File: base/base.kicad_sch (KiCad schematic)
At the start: 0 parts

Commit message: base: DF40 receptacle + DIP48 socket, schematic drawn and wired
Board B goes DF40 mezzanine -> 48-pin DIP socket (female). The XGecu
adapter carries the male DIP48 pins and inserts from above; both are
viewed from the top so the socket is not mirrored, unlike the DF40 pair.

Stack height is 1.5 mm, forced by the plug already on the carrier.
DF40GB is the shielded family, and per the DF40 catalog it offers 30
positions at 1.5 mm only, with DF40GB(1.5)-30DS-0.4V(51) as the sole
mating receptacle. No DF40 family reaches 4.0 mm at 30 positions; that
starts at 50. Unshielded DF40C/HC would reach 3.5 mm but need a new plug
on the carrier.

New parts:
- HIROSE_DF40GB-30DS-0.4V_51_ footprint, from catalog p.12 Recommended
  PCB Pattern: signal 0.2 x 0.70 at y +-1.54, ground 0.28 x 0.72 at
  x +-3.24 / y +-1.68. Mirrored in X, pin 1 at +X, for the face-to-face
  mate.
- DIP-48_Socket_W15.24mm_P2.54mm, 48 THT, 0.9 drill / 1.6 pad, 0.6in
  rows, 58.42 mm pin 1 to pin 24.
- DF40GB-30DS-0.4V_51_ and DIP-48_Socket symbols.
- base/lib registered in both library tables.

base.kicad_sch: J1 receptacle, J2 socket, 10k pull-ups on RY//BY and
/WP, 1 uF bulk + 100 nF, PWR_FLAGs since power arrives through J2.
ERC 0 violations. 17 nets, every one cross-checked against both tables
in docs/connector-pinout.md.

Docs corrected: the "schematic is drawn and wired" claim, the netclass
pattern table, the stack height, and the mating-face description.

Co-Authored-By: Claude Opus 5 <noreply@anthropic.com>
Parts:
- added C1: 1uF, Capacitor_SMD:C_0603_1608Metric, symbol Device:C
- added C2: 100nF, Capacitor_SMD:C_0402_1005Metric, symbol Device:C
- added J1: DF40GB(1.5)-30DS-0.4V(51), Connector_Hirose_DF40:HIROSE_DF40GB-30DS-0.4V_51_, symbol carrier:DF40GB-30DS-0.4V_51_
- added J2: DIP-48_Socket, base:DIP-48_Socket_W15.24mm_P2.54mm, symbol base:DIP-48_Socket
- added R1, R2: 10k, Resistor_SMD:R_0402_1005Metric, symbol Device:R
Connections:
- new net ALE: J1.12, J2.17 (ALE)
- new net CLE: J1.8, J2.16 (CLE)
- new net GND: C1.2, C2.2, J1.10, J1.11, J1.14, J1.18, J1.2, J1.22, J1.23, J1.26, J1.27, J1.3, J1.30, J1.6, J1.7, J1.G1 (GND), J1.G2 (GND), J1.G3 (GND), J1.G4 (GND), J2.13 (VSS), J2.36 (VSS)
- new net IO1: J1.1, J2.29 (I/O1)
- new net IO2: J1.5, J2.30 (I/O2)
- new net IO3: J1.9, J2.31 (I/O3)
- new net IO4: J1.13, J2.32 (I/O4)
- new net IO5: J1.17, J2.41 (I/O5)
- new net IO6: J1.21, J2.42 (I/O6)
- new net IO7: J1.25, J2.43 (I/O7)
- new net IO8: J1.29, J2.44 (I/O8)
- new net RY//BY: J1.28, J2.7 (RY/~{BY}), R1.2
- new net VCC: C1.1, C2.1, J1.15, J1.19, J2.12 (VCC), J2.37 (VCC), R1.1, R2.1
- new net /CE: J1.4, J2.9 (~{CE})
- new net /RE: J1.20, J2.8 (~{RE})
- new net /WE: J1.16, J2.18 (~{WE})
- new net /WP: J1.24, J2.19 (~{WP}), R2.2
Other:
- company: (none) -> Alex Gompper
- title: (none) -> DF40 Mezzanine to DIP48 Socket

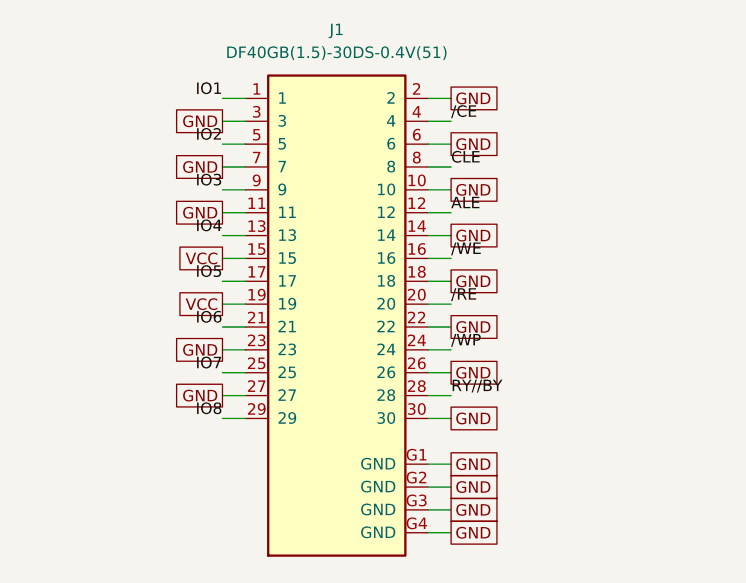
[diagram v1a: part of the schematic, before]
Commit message: Re-derive the J1 pinout from ball geometry; regenerate both schematics
Alex asked to optimise J1's pin assignment for the BGA fanout, and to
consider routing on the inner layers working back from J1 rather than
out from U1. Working backwards is what produced the result.

The topology falls out of the ball map with no slack. The VFBGA67's 20
used balls split into an upper cluster (columns 2-4: IO1-IO4 plus
CLE/RE/ALE/WP) and a lower one (columns 5-7: IO5-IO8, CE/WE/RY-BY and
both VCC balls) - exactly 8 and 7 signals. J1's odd row has exactly 8
signal slots and its even row exactly 7. So the row assignment is
forced, and within a row ordering by ball x makes the escape fan out
monotonically. IO1-IO8 are no longer in pin order on the connector;
that is deliberate and safe, because the rule that matters is the
end-to-end mapping, not the connector order.

Measured against the previous pinout with a routing-aware cost model
(octilinear where clear, around-the-end where the connector body is in
the way): 141.2 mm -> 74.8 mm of point-to-point routing, IO skew
10.32 mm -> 2.94 mm, and around-the-end paths 11 -> 5. Constraining the
bus to stay contiguous recovers almost none of that (139.6 mm), because
the IO balls all sit on one side while a monotonic bus spans J1's full
5.6 mm.

Skew was not the reason to do this. 10 mm is ~62 ps on FR4 against a
25 ns read cycle. The win is copper length and via count.

tools/pinout.py is now the single source: it carries the table and a
checker for the checkerboard invariant (no signal adjacent to or
opposite another signal) and the net set. Both schematics were
generated from it. Verified: carrier ERC 0, base ERC 0, both J1s match
the table, U1 matches the datasheet ball map, J2 matches the TSOP48
map, and IOn traces ball -> J1 pin -> TSOP48 pin end to end.

Carrier PCB carries placement, net re-import and the BGA escape (20/20
balls, DRC 0 errors). The J1 fanout is NOT routed in this commit - see
the next commit message / handoff for w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
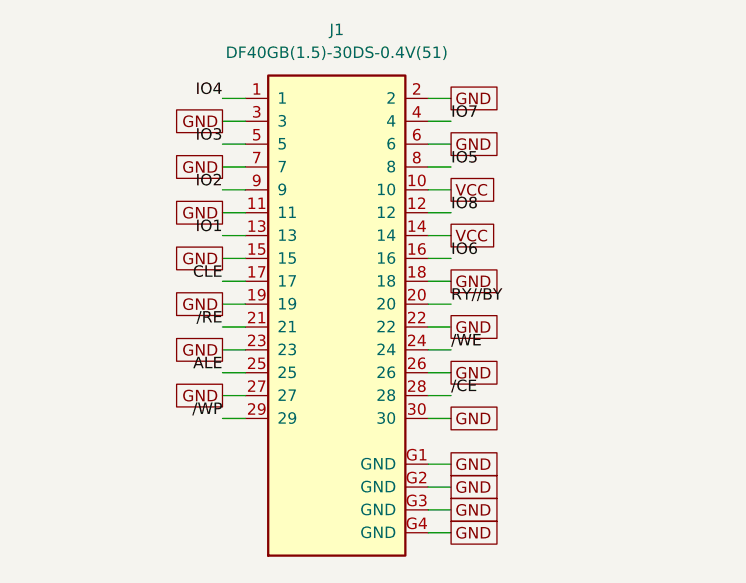
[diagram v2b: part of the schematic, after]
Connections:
- net ALE: now also J1.25; no longer J1.12
- net CLE: now also J1.17; no longer J1.8
- net GND: now also J1.15, J1.19; no longer J1.10, J1.14
- net IO1: now also J1.13; no longer J1.1
- net IO2: now also J1.9; no longer J1.5
- net IO3: now also J1.5; no longer J1.9
- net IO4: now also J1.1; no longer J1.13
- net IO5: now also J1.8; no longer J1.17
- net IO6: now also J1.16; no longer J1.21
- net IO7: now also J1.4; no longer J1.25
- net IO8: now also J1.12; no longer J1.29
- net RY//BY: now also J1.20; no longer J1.28
- net VCC: now also J1.10, J1.14; no longer J1.15, J1.19
- net /CE: now also J1.28; no longer J1.4
- net /RE: now also J1.21; no longer J1.20
- net /WE: now also J1.24; no longer J1.16
- net /WP: now also J1.29; no longer J1.24

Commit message: Carrier fully routed; propagate the VCC pin move to base and the docs
Alex routed the carrier: 0 DRC violations, 0 unconnected, one via per
signal net (20 total), uniform 0.15 mm tracks, teardrops on every
via/pad transition, GND poured on all four layers.

While routing he moved VCC from J1 pin 14 to pin 6, which is the right
call - pin 6's x lines up with the VCC ball H5, and pin 10 already lined
up with G7. But the change landed on the carrier only, so pin 6 was VCC
on one board and GND on the other, and pin 14 the reverse. Mated, that
is VCC shorted to GND through two pins.

Neither project can catch this: they are separate KiCad projects, so
each one's ERC and DRC pass happily. This is exactly the failure the
"single source of truth" note in the pinout doc exists to prevent.

Adopted the carrier's version as canonical: tools/pinout.py now has
VCC on 6 and 10, base regenerated from it, doc table updated. The
checkerboard invariant still holds. Verified both J1s now agree on all
34 pins including the G tabs.

carrier ERC 0, base ERC 0, carrier DRC 0 violations / 0 unconnected.

Co-Authored-By: Claude Opus 5 <noreply@anthropic.com>
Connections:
- net GND: now also J1.14; no longer J1.6
- net VCC: now also J1.6; no longer J1.14
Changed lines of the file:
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@@
 		(property "Value" "DF40GB(1.5)-30DS-0.4V(51)" (at 63.5 40.64 0) (effects (font (size 1.27 1.27))))
 		(property "Footprint" "Connector_Hirose_DF40:HIROSE_DF40GB-30DS-0.4V_51_" (at 63.5 63.5 0) (effects (font (size 1.27 1.27)) (hide yes)))
-		(instances (project "base" (path "/5f6296ef-f47b-4b20-84d4-3df797b20810" (reference "J1") (unit 1))))
+		(instances (project "base" (path "/14e6b38a-f306-41d1-a4e0-ab6ee141c397" (reference "J1") (unit 1))))
 	)
 	(wire (pts (xy 50.8 45.72) (xy 53.34 45.72)) (stroke (width 0) (type default)))
@@
 	(label "IO3" (at 50.8 50.8 0) (effects (font (size 1.27 1.27)) (justify right bottom)))
 	(wire (pts (xy 73.66 50.8) (xy 76.2 50.8)) (stroke (width 0) (type default)))
-	(global_label "GND" (shape passive) (at 76.2 50.8 0) (effects (font (size 1.27 1.27)) (justify left)))
+	(global_label "VCC" (shape passive) (at 76.2 50.8 0) (effects (font (size 1.27 1.27)) (justify left)))
 	(wire (pts (xy 50.8 53.339999999999996) (xy 53.34 53.339999999999996)) (stroke (width 0) (type default)))
 	(global_label "GND" (shape passive) (at 50.8 53.339999999999996 0) (effects (font (size 1.27 1.27)) (justify right)))
@@
 	(label "IO1" (at 50.8 60.96 0) (effects (font (size 1.27 1.27)) (justify right bottom)))
 	(wire (pts (xy 73.66 60.96) (xy 76.2 60.96)) (stroke (width 0) (type default)))
-	(global_label "VCC" (shape passive) (at 76.2 60.96 0) (effects (font (size 1.27 1.27)) (justify left)))
+	(global_label "GND" (shape passive) (at 76.2 60.96 0) (effects (font (size 1.27 1.27)) (justify left)))
 	(wire (pts (xy 50.8 63.5) (xy 53.34 63.5)) (stroke (width 0) (type default)))
 	(global_label "GND" (shape passive) (at 50.8 63.5 0) (effects (font (size 1.27 1.27)) (justify right)))
@@
 		(property "Value" "DIP-48_Socket" (at 152.4 41.3 0) (effects (font (size 1.27 1.27))))
 		(property "Footprint" "base:DIP-48_Socket_W15.24mm_P2.54mm" (at 152.4 50.8 0) (effects (font (size 1.27 1.27)) (hide yes)))
-		(instances (project "base" (path "/5f6296ef-f47b-4b20-84d4-3df797b20810" (reference "J2") (unit 1))))
+		(instances (project "base" (path "/14e6b38a-f306-41d1-a4e0-ab6ee141c397" (reference "J2") (unit 1))))
 	)
 	(wire (pts (xy 149.86 66.03999999999999) (xy 152.4 66.03999999999999)) (stroke (width 0) (type default)))
@@
 		(property "Value" "10k" (at 34.88 128.27 0) (effects (font (size 1.27 1.27))))
 		(property "Footprint" "Resistor_SMD:R_0402_1005Metric" (at 30.48 127.0 0) (effects (font (size 1.27 1.27)) (hide yes)))
-		(instances (project "base" (path "/5f6296ef-f47b-4b20-84d4-3df797b20810" (reference "R1") (unit 1))))
+		(instances (project "base" (path "/14e6b38a-f306-41d1-a4e0-ab6ee141c397" (reference "R1") (unit 1))))
 	)
 	(wire (pts (xy 30.48 123.19) (xy 30.48 120.65)) (stroke (width 0) (type default)))
@@
 		(property "Value" "10k" (at 50.12 128.27 0) (effects (font (size 1.27 1.27))))
 		(property "Footprint" "Resistor_SMD:R_0402_1005Metric" (at 45.72 127.0 0) (effects (font (size 1.27 1.27)) (hide yes)))
-		(instances (project "base" (path "/5f6296ef-f47b-4b20-84d4-3df797b20810" (reference "R2") (unit 1))))
+		(instances (project "base" (path "/14e6b38a-f306-41d1-a4e0-ab6ee141c397" (reference "R2") (unit 1))))
 	)
 	(wire (pts (xy 45.72 123.19) (xy 45.72 120.65)) (stroke (width 0) (type default)))
@@
 		(property "Value" "1uF" (at 65.36 128.27 0) (effects (font (size 1.27 1.27))))
 		(property "Footprint" "Capacitor_SMD:C_0603_1608Metric" (at 60.96 127.0 0) (effects (font (size 1.27 1.27)) (hide yes)))
-		(instances (project "base" (path "/5f6296ef-f47b-4b20-84d4-3df797b20810" (reference "C1") (unit 1))))
+		(instances (project "base" (path "/14e6b38a-f306-41d1-a4e0-ab6ee141c397" (reference "C1") (unit 1))))
 	)
 	(wire (pts (xy 60.96 123.19) (xy 60.96 120.65)) (stroke (width 0) (type default)))
@@
 		(property "Value" "100nF" (at 80.60000000000001 128.27 0) (effects (font (size 1.27 1.27))))
 		(property "Footprint" "Capacitor_SMD:C_0402_1005Metric" (at 76.2 127.0 0) (effects (font (size 1.27 1.27)) (hide yes)))
-		(instances (project "base" (path "/5f6296ef-f47b-4b20-84d4-3df797b20810" (reference "C2") (unit 1))))
+		(instances (project "base" (path "/14e6b38a-f306-41d1-a4e0-ab6ee141c397" (reference "C2") (unit 1))))
 	)
 	(wire (pts (xy 76.2 123.19) (xy 76.2 120.65)) (stroke (width 0) (type default)))
@@
 		(property "Reference" "#FLG01" (at 99.06 115.0 0) (effects (font (size 1.27 1.27)) (hide yes)))
 		(property "Value" "PWR_FLAG" (at 99.06 117.5 0) (effects (font (size 1.27 1.27)) (hide yes)))
-		(instances (project "base" (path "/5f6296ef-f47b-4b20-84d4-3df797b20810" (reference "#FLG01") (unit 1))))
+		(instances (project "base" (path "/14e6b38a-f306-41d1-a4e0-ab6ee141c397" (reference "#FLG01") (unit 1))))
 	)
 	(wire (pts (xy 99.06 127.0) (xy 99.06 121.92)) (stroke (width 0) (type default)))
@@
 		(property "Reference" "#FLG02" (at 114.3 115.0 0) (effects (font (size 1.27 1.27)) (hide yes)))
 		(property "Value" "PWR_FLAG" (at 114.3 117.5 0) (effects (font (size 1.27 1.27)) (hide yes)))
-		(instances (project "base" (path "/5f6296ef-f47b-4b20-84d4-3df797b20810" (reference "#FLG02") (unit 1))))
+		(instances (project "base" (path "/14e6b38a-f306-41d1-a4e0-ab6ee141c397" (reference "#FLG02") (unit 1))))
 	)
 	(wire (pts (xy 114.3 127.0) (xy 114.3 121.92)) (stroke (width 0) (type default)))
